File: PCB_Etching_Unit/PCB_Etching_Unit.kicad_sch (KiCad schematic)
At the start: 83 parts, among them M1 Motor_DC, M2 Motor_DC, Q1 TIP42, Q10 TIP42, Q11 TIP41, Q12 2N3904, Q13 TIP42, Q14 BC550, Q15 BC550, Q16 BC550, Q17 BC550, Q18 BC550, Q19 BC550, Q2 TIP42, Q20 BC550, Q3 TIP42, Q4 TIP42, Q5 TIP42, Q6 TIP41, Q7 TIP41, Q8 TIP42, Q9 TIP41, SW1 SW_MEC_5G, SW2 SW_MEC_5G, SW4 SW_MEC_5G, SW5 SW_MEC_5G, SW6 SW_MEC_5G, U1 HDSP-7801, U11 4511, U2 HDSP-7801, U3 HDSP-7801, U4 HDSP-7801, U5 4027, U6 4027, U9 4011

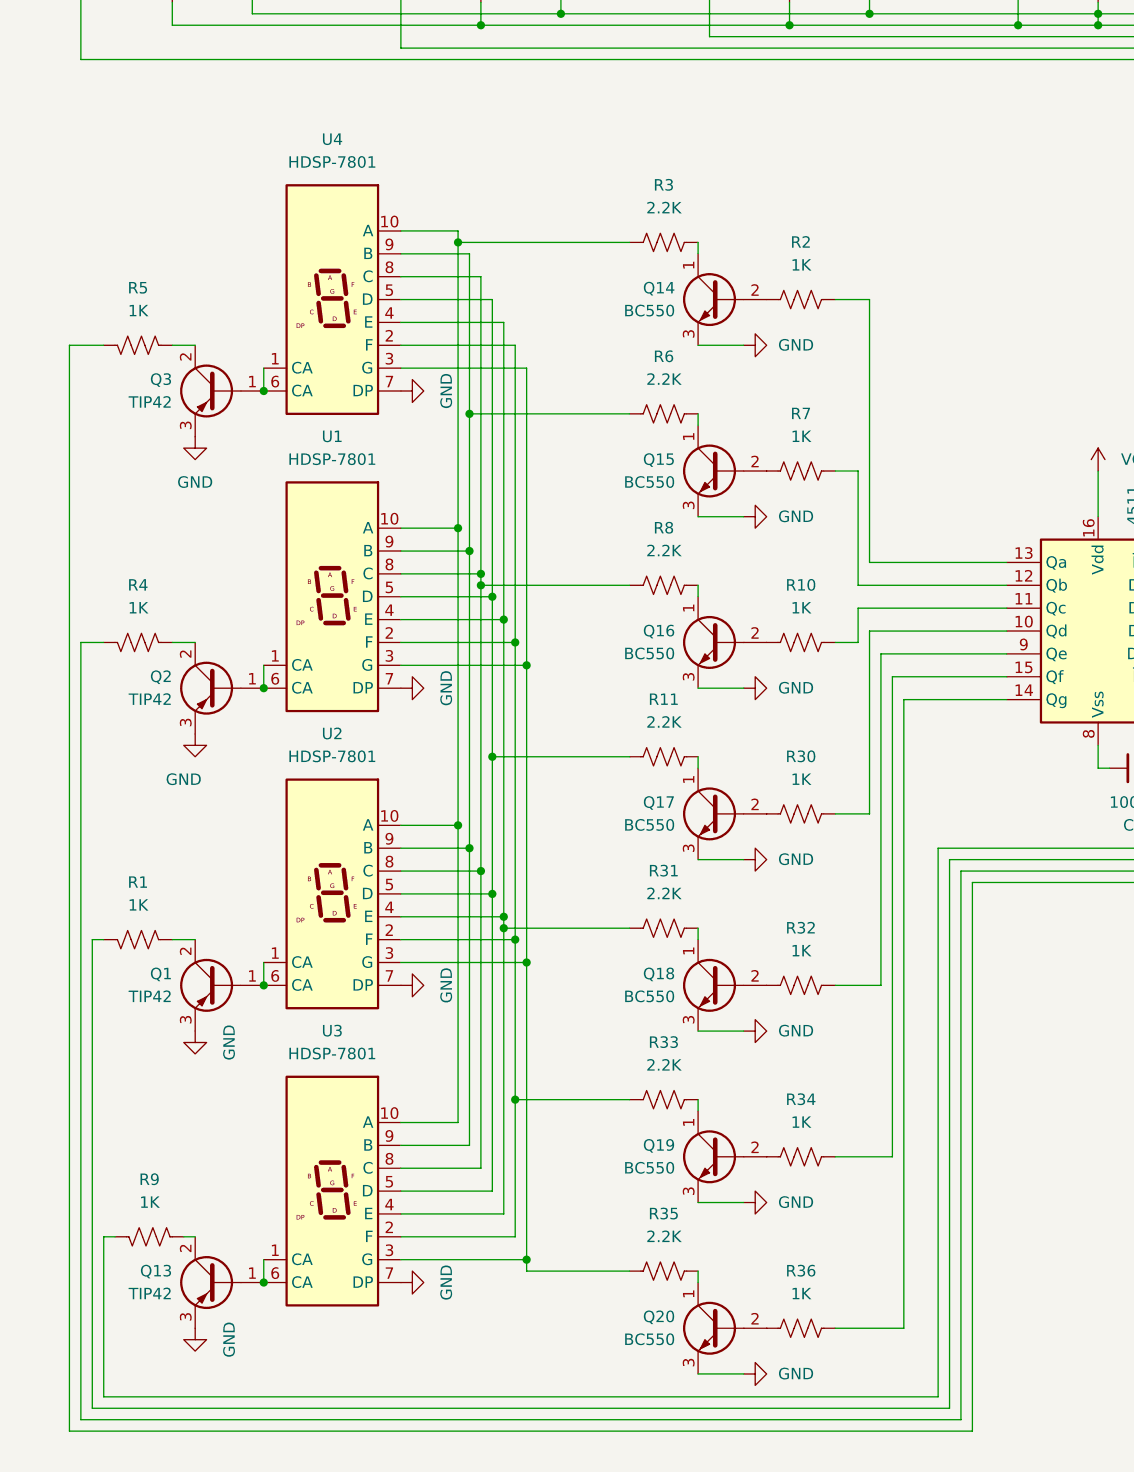
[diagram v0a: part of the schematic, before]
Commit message: Fixed wrong pnp, npn bjt orientation of 7-segment-display.
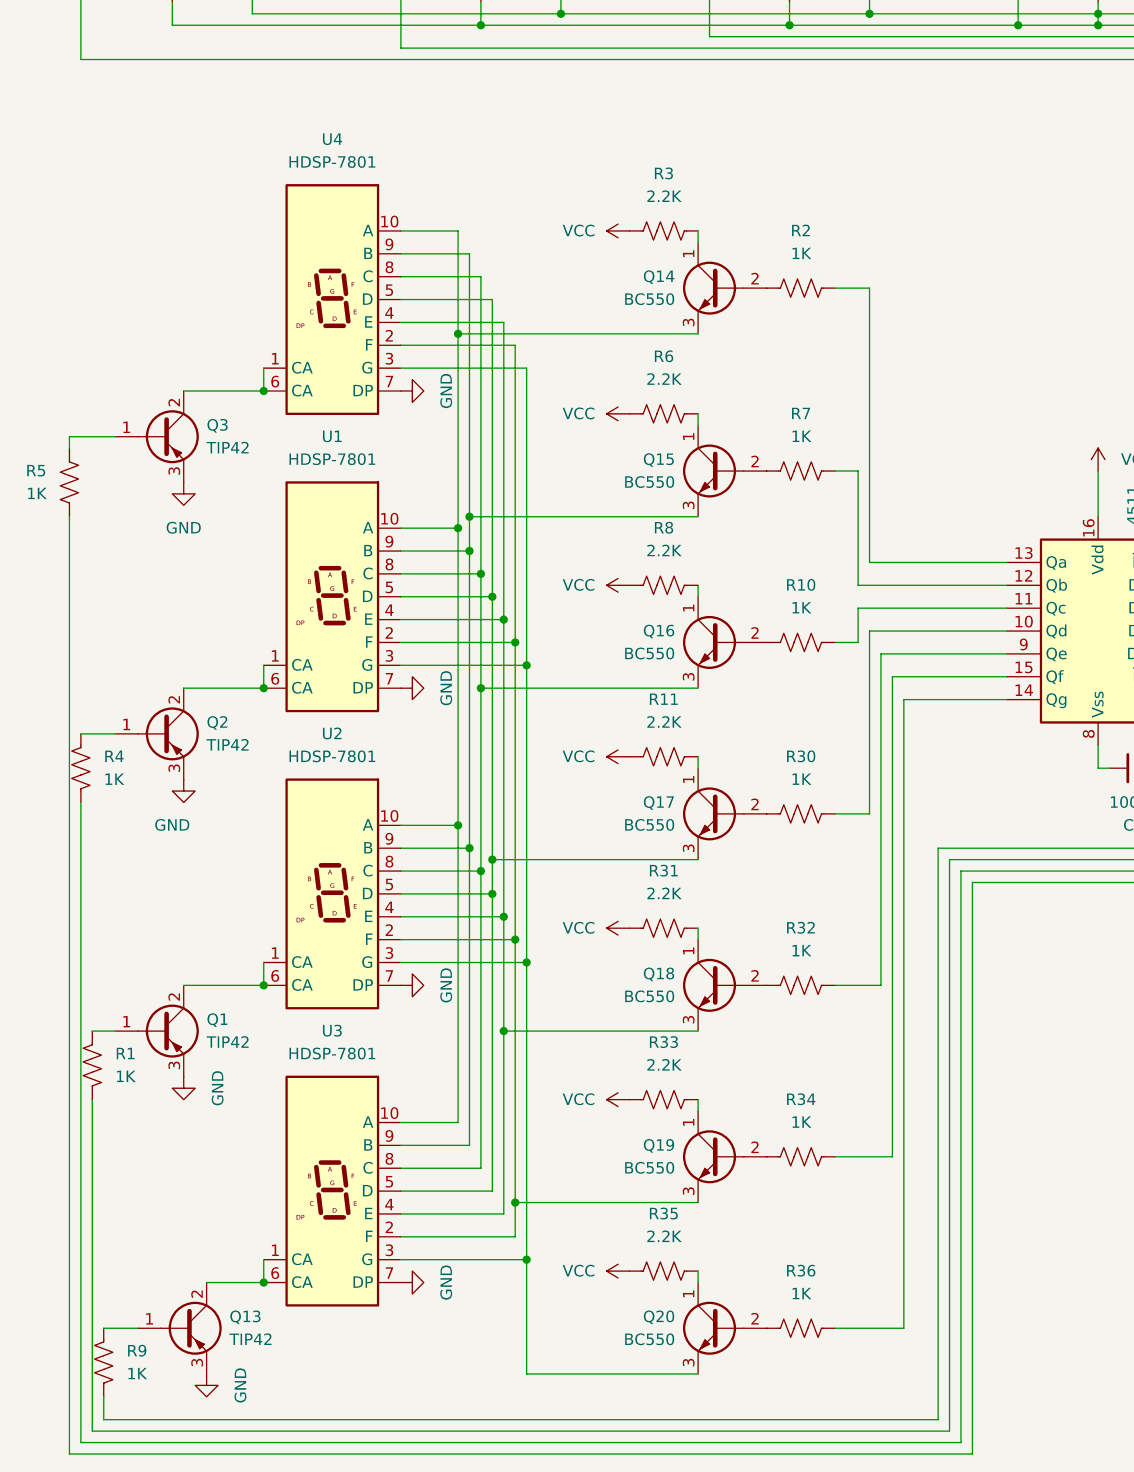
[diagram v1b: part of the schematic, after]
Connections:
- net GND: no longer Q14.3 (E), Q15.3 (E), Q16.3 (E), Q17.3 (E), Q18.3 (E), Q19.3 (E), Q20.3 (E)
- net VCC: now also R11.1, R3.2, R31.1, R33.1, R35.1, R6.1, R8.1
- net at R1.1: now also Q1.1 (B); no longer Q1.2 (C)
- net at R4.1: now also Q2.1 (B); no longer Q2.2 (C)
- net at U1.9 (B), U2.9 (B), U3.9 (B)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: now also Q15.3 (E); no longer R6.1
- net at R5.1: now also Q3.1 (B); no longer Q3.2 (C)
- net at U3.1 (CA), U3.6 (CA): now also Q13.2 (C); no longer Q13.1 (B)
- net at R9.1: now also Q13.1 (B); no longer Q13.2 (C)
- net at Q14.1 (C): now also R3.1; no longer R3.2
- net at U4.1 (CA), U4.6 (CA): now also Q3.2 (C); no longer Q3.1 (B)
- net at U1.3 (G), U2.3 (G), U3.3 (G)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: now also Q20.3 (E); no longer R35.1
- net at U1.1 (CA), U1.6 (CA): now also Q2.2 (C); no longer Q2.1 (B)
- net at U1.4 (E), U2.4 (E), U3.4 (E)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: now also Q18.3 (E); no longer R31.1
- net at U2.1 (CA), U2.6 (CA): now also Q1.2 (C); no longer Q1.1 (B)
- net at U1.10 (A), U2.10 (A), U3.10 (A)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: now also Q14.3 (E); no longer R3.1
- net at U1.2 (F), U2.2 (F), U3.2 (F)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: now also Q19.3 (E); no longer R33.1
- net at U1.5 (D), U2.5 (D), U3.5 (D)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: now also Q17.3 (E); no longer R11.1
- net at U1.8 (C), U2.8 (C), U3.8 (C)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: now also Q16.3 (E); no longer R8.1
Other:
- moved on the sheet: Q1, Q13, Q14, Q2, Q3, R1, R2, R3, R4, R5, R9

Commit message: Added label definitions and moved some parts around.
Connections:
- net UP: no longer A1.9 (A0)
- net at R20.2, R26.2: now also A1.25 (D10); no longer A1.27 (D12)
- net at R19.2, R21.2: now also A1.26 (D11); no longer A1.28 (D13)
- net BZ-STOP renamed ALARM-STOP
- net SAVE renamed START-SAVE
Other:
- moved on the sheet: C1, D1, D2, D3, D4, D5, D6, D7, D8, M1, M2, Q10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

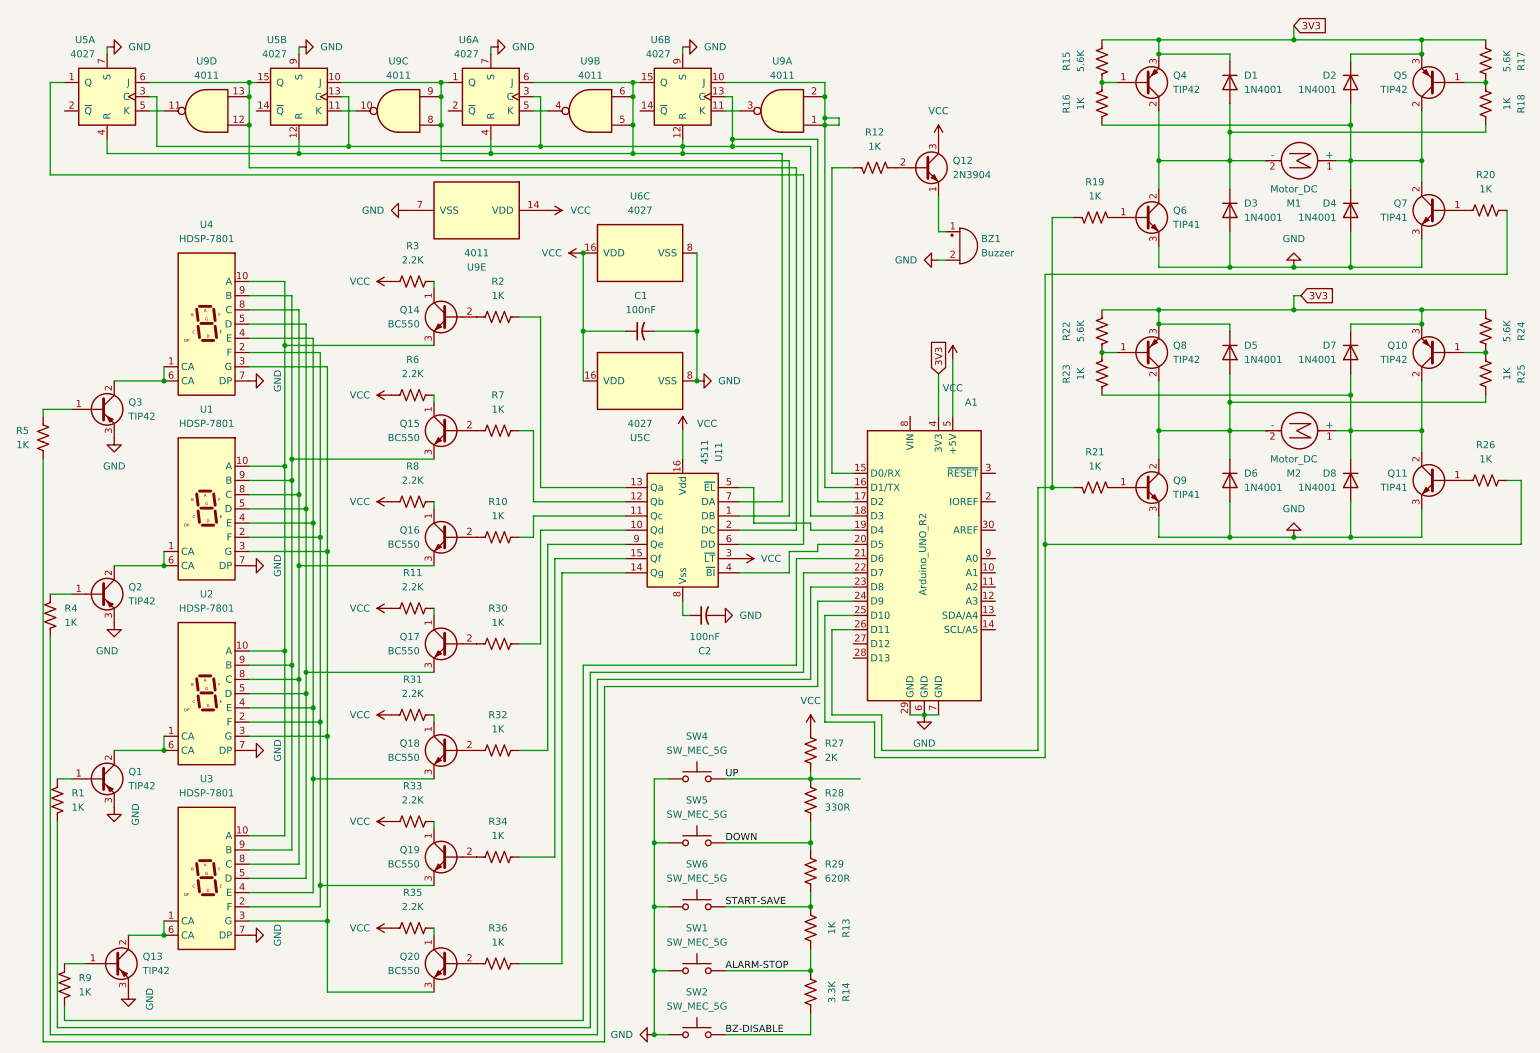
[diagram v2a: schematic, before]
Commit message: Added poti for speed control and manual mode button.
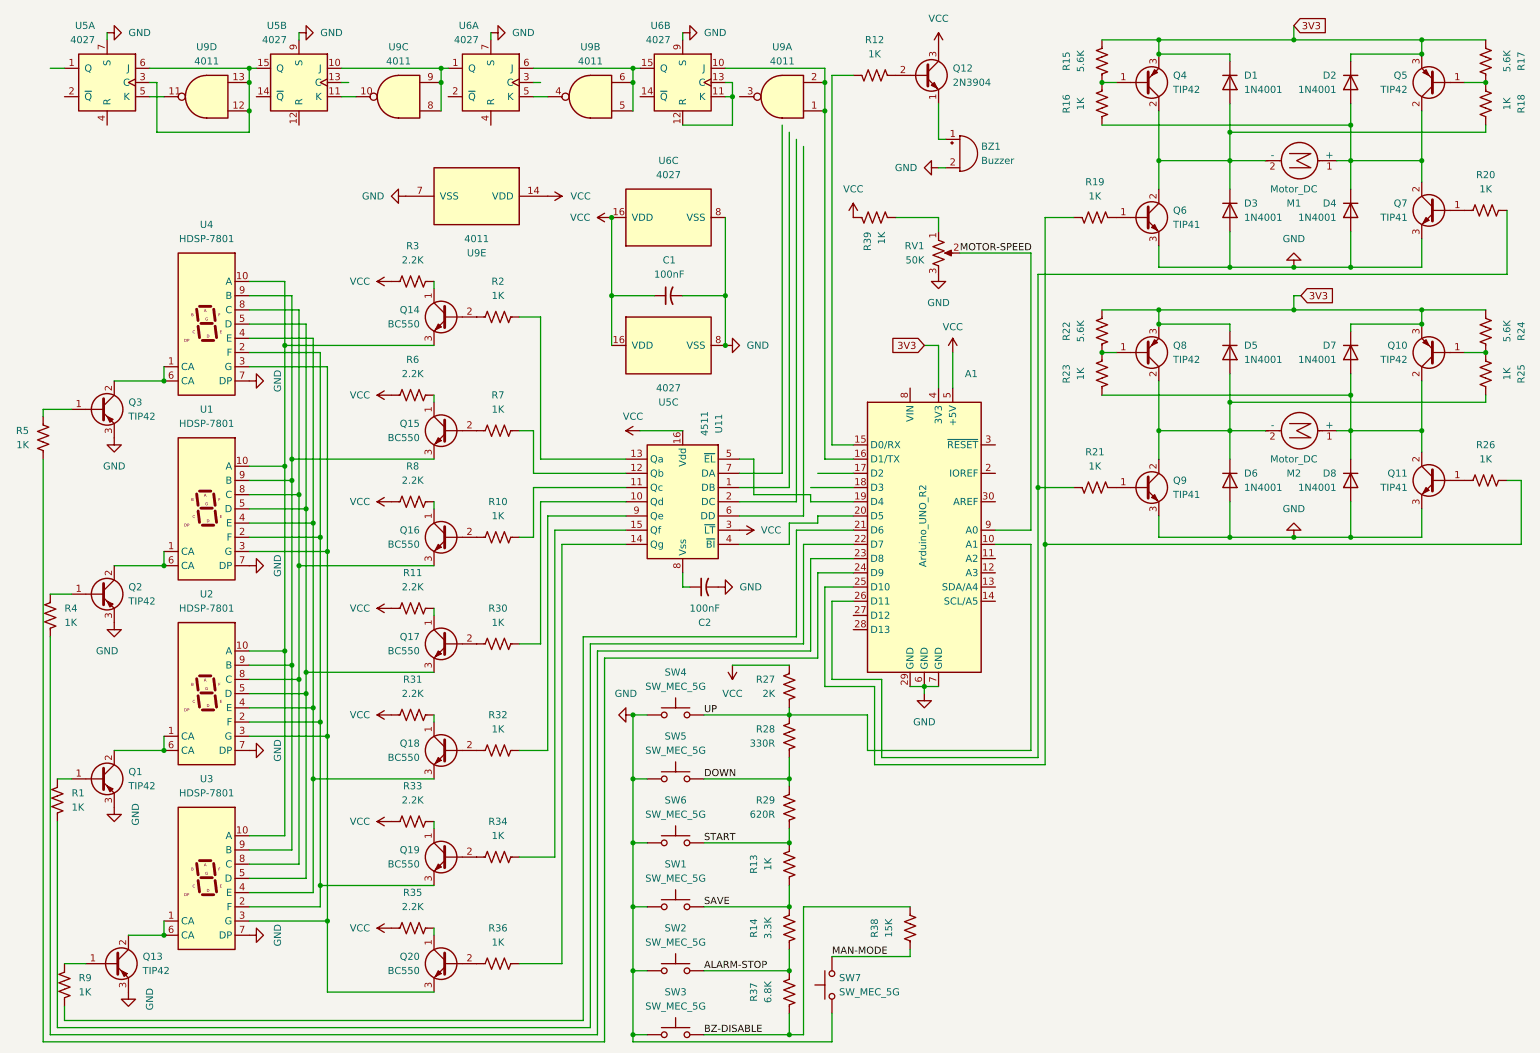
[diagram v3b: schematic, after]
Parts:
- added R37: 6.8K, Resistor_THT:R_Axial_DIN0204_L3.6mm_D1.6mm_P7.62mm_Horizontal, symbol Device:R_US
- added R38: 15K, Resistor_THT:R_Axial_DIN0204_L3.6mm_D1.6mm_P7.62mm_Horizontal, symbol Device:R_US
- added R39: 1K, Resistor_THT:R_Axial_DIN0204_L3.6mm_D1.6mm_P7.62mm_Horizontal, symbol Device:R_US
- added RV1: 50K, Potentiometer_SMD:Potentiometer_Bourns_3214G_Horizontal, symbol Device:R_Potentiometer_US
- added SW3, SW7: SW_MEC_5G, Button_Switch_SMD:SW_MEC_5GSH9, symbol Switch:SW_MEC_5G
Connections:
- net ALARM-STOP: now also R14.2, SW2.1 (A), SW2.2 (A), R37.1; no longer R13.2, R14.1, SW1.1 (A), SW1.2 (A)
- net BZ-DISABLE: now also R37.2, R38.2, SW3.1 (A), SW3.2 (A); no longer R14.2, SW2.1 (A), SW2.2 (A)
- net GND: now also RV1.3, SW3.3 (B), SW3.4 (B), SW7.3 (B), SW7.4 (B)
- net UP: now also A1.10 (A1)
- net VCC: now also R39.2
- net at A1.25 (D10), R26.2: now also R19.2; no longer R20.2
- net at U5.15 (Q), U5.6 (J), U9.12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: now also U5.3 (C); no longer U11.2 (DC)
- net at U5.10 (J), U6.1 (Q), U9.8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: no longer U11.1 (DB)
- net at U9.3: no longer U6.11 (K)
- net at A1.26 (D11), R21.2: now also R20.2; no longer R19.2
- net at U11.6 (DD): no longer U5.1 (Q)
- net MOTOR-SPEED: now reaches A1.9 (A0)
- net MOTOR-SPEED: now also RV1.2
- net START-SAVE renamed START
- new net: R39.1, RV1.1
- new net: U6.11 (K), U6.12 (R), U6.13 (C)
- new net: U6.15 (Q), U6.6 (J), U9.5, U9.6
- new net MAN-MODE: R38.1, SW7.1 (A), SW7.2 (A)
- new net SAVE: R13.2, R14.1, SW1.1 (A), SW1.2 (A)
- now unconnected: A1.17 (D2), A1.18 (D3), U11.7 (DA), U5.12 (R), U5.13 (C), U5.4 (R), U6.3 (C), U6.4 (R)
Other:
- moved on the sheet: A1, BZ1, C1, C2, Q12, R12, R13, R14, R27, R28, R29, SW1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
